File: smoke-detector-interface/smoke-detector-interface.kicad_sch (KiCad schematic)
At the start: 28 parts, among them J1 Conn_01x04_Pin, J2 M50-3500542, J3 DE9_Receptacle, J4 61200621621, J5 Conn_01x06_Pin, U1 UA78L10ACLPRE3, U2 AS7805AT, U3 ATtiny13A-P

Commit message: WIP
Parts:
- JP1: footprint TestPoint:TestPoint_Bridge_Pitch2.54mm_Drill0.7mm -> Resistor_THT:R_Axial_DIN0204_L3.6mm_D1.6mm_P7.62mm_Horizontal
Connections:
- net HOSTRX: now also J5.4 (Pin_4); no longer JP1.1 (A)
- net HOSTTX: now also JP1.1 (A); no longer J5.3 (Pin_3)
- net at JP1.2 (B): now also J5.3 (Pin_3); no longer J5.4 (Pin_4)
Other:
- moved on the sheet: JP1
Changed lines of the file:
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@@
 	(wire
 		(pts
-			(xy 196.85 143.51) (xy 194.31 143.51)
+			(xy 194.31 143.51) (xy 208.28 143.51)
 		)
 		(stroke
@@
 	(wire
 		(pts
-			(xy 208.28 140.97) (xy 196.85 140.97)
+			(xy 208.28 140.97) (xy 207.01 140.97)
 		)
 		(stroke
@@
 	(wire
 		(pts
-			(xy 208.28 143.51) (xy 207.01 143.51)
-		)
-		(stroke
-			(width 0)
-			(type default)
-		)
-	)
-	(wire
-		(pts
 			(xy 231.14 88.9) (xy 231.14 91.44)
 		)
@@
 	(symbol
 		(lib_id "Jumper:Jumper_2_Open")
-		(at 201.93 143.51 0)
+		(at 201.93 140.97 0)
 		(unit 1)
 		(exclude_from_sim yes)
@@
 		(fields_autoplaced yes)
 		(property "Reference" "JP1"
-			(at 201.93 137.16 0)
+			(at 201.93 134.62 0)
 			(effects
 				(font
@@
 		)
 		(property "Value" "Jumper_2_Open"
-			(at 201.93 139.7 0)
+			(at 201.93 137.16 0)
 			(effects
 				(font
@@
 			)
 		)
-		(property "Footprint" "TestPoint:TestPoint_Bridge_Pitch2.54mm_Drill0.7mm"
-			(at 201.93 143.51 0)
+		(property "Footprint" "Resistor_THT:R_Axial_DIN0204_L3.6mm_D1.6mm_P7.62mm_Horizontal"
+			(at 201.93 140.97 0)
 			(effects
 				(font
@@
 		)
 		(property "Datasheet" "~"
-			(at 201.93 143.51 0)
+			(at 201.93 140.97 0)
 			(effects
 				(font
@@
 		)
 		(property "Description" "Jumper, 2-pole, open"
-			(at 201.93 143.51 0)
+			(at 201.93 140.97 0)
 			(effects
 				(font

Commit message: Improved routing.
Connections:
- net _RESET: now also J4.5, U3.1 (~{RESET}/PB5)
- net MOSI: now reaches J4.4, U3.5 (PB0)
- net MISO: now reaches J4.1, U3.6 (PB1)
- net SCK: now reaches J4.3, U3.7 (PB2)
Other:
- moved on the sheet: J4, J5, JP1

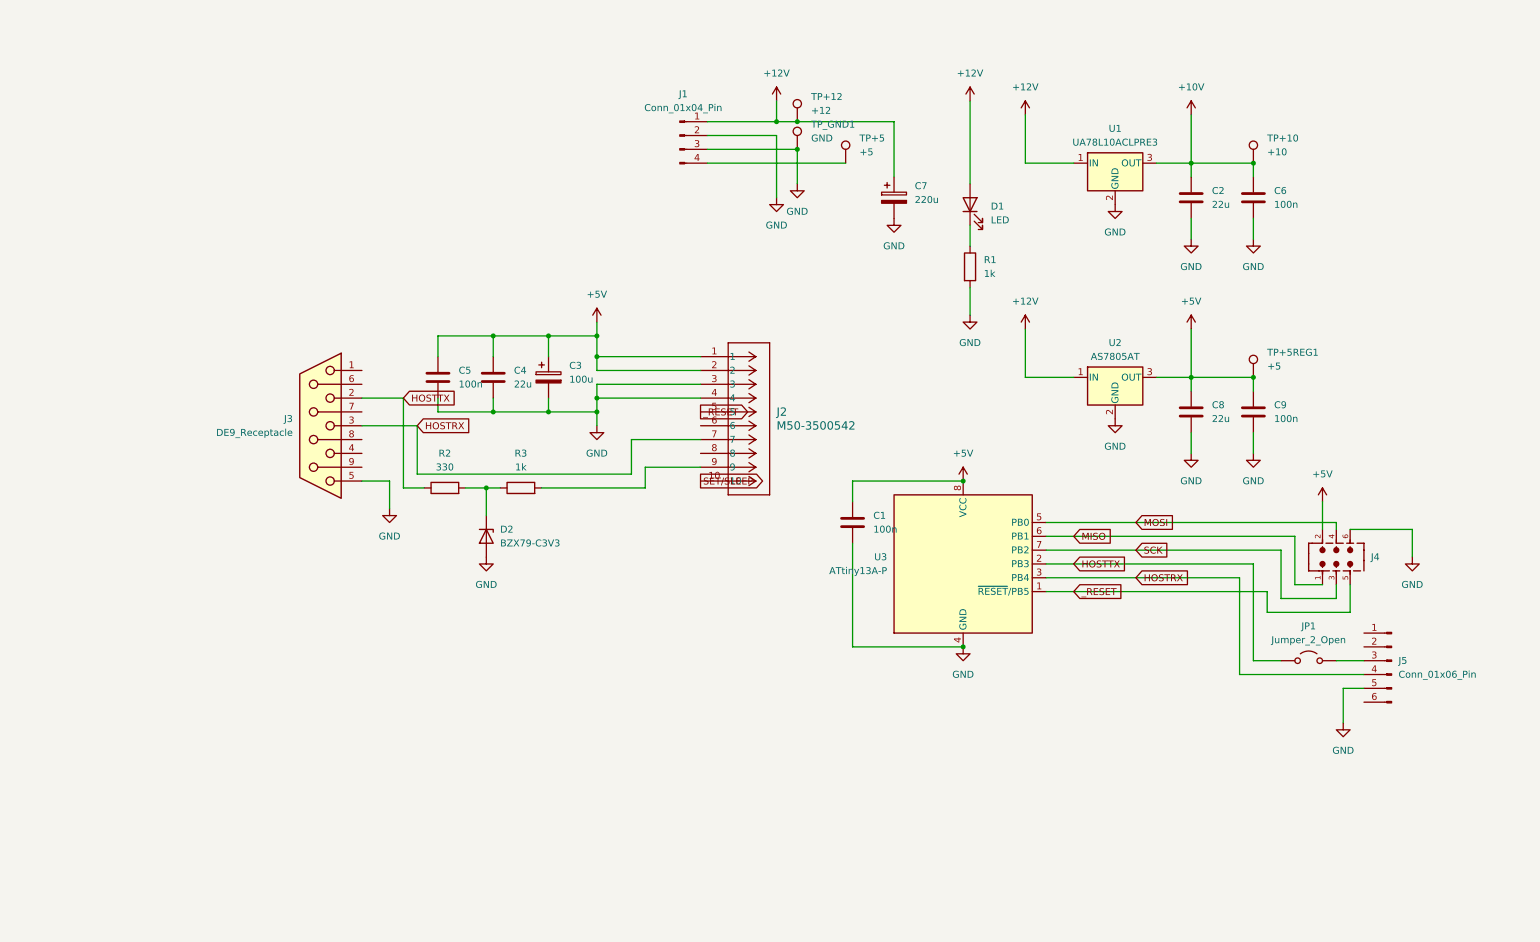
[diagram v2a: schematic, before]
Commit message: Updates for Zenerglass parts.
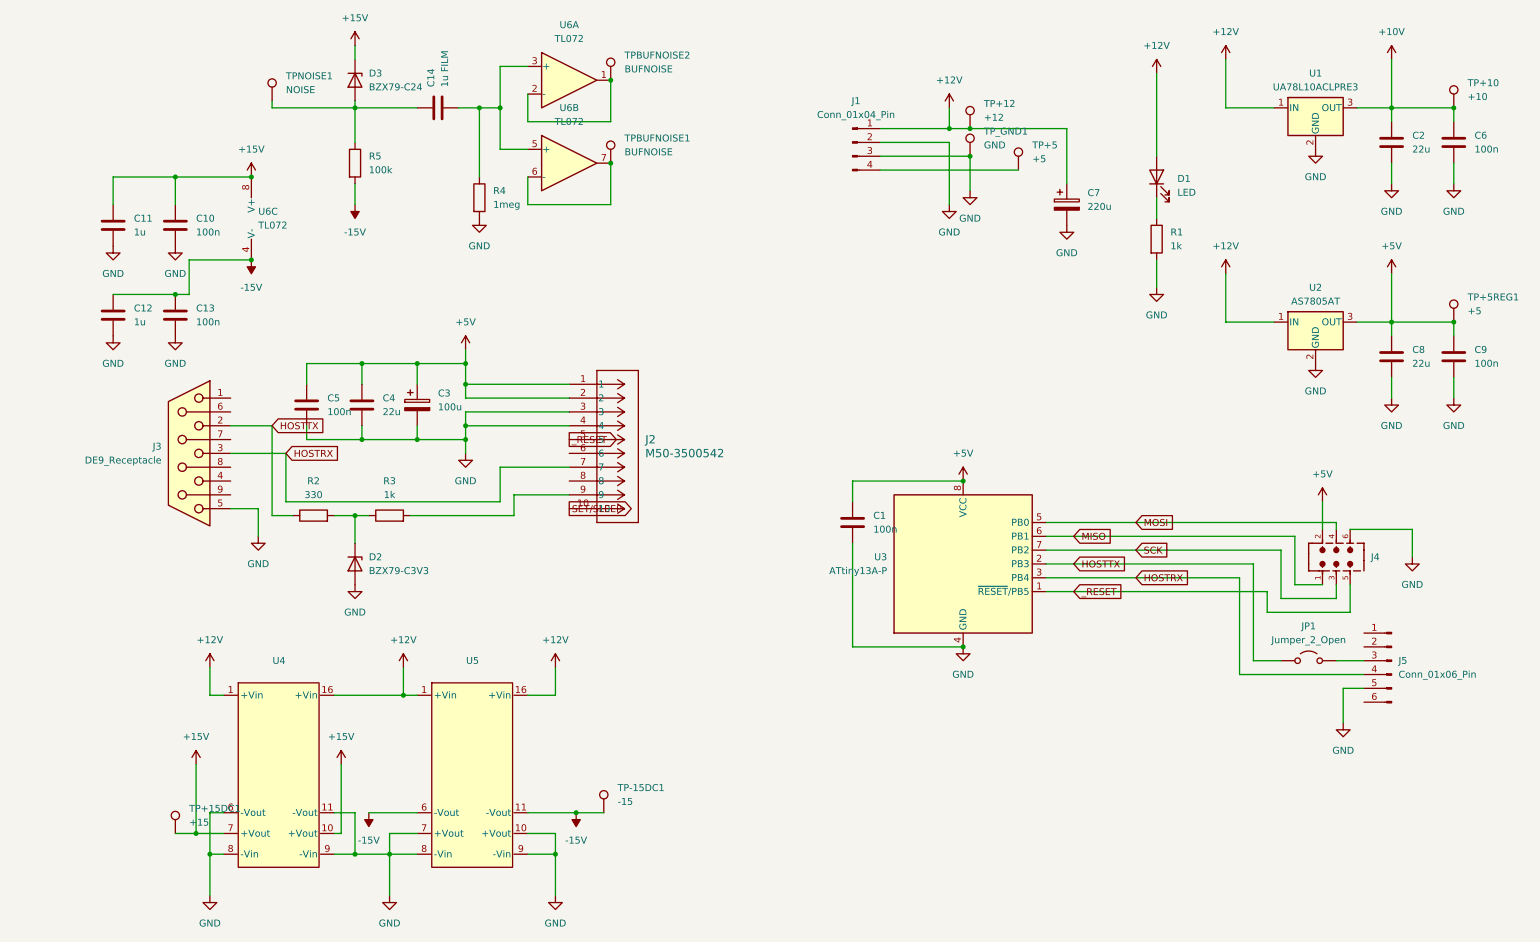
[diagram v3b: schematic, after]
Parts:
- added C10, C13: 100n, Capacitor_THT:C_Disc_D4.3mm_W1.9mm_P5.00mm, symbol Device:C
- added C11, C12: 1u, Capacitor_THT:C_Disc_D4.3mm_W1.9mm_P5.00mm, symbol Device:C
- added C14: 1u FILM, Capacitor_THT:C_Disc_D4.3mm_W1.9mm_P5.00mm, symbol Device:C
- added D3: BZX79-C24, Diode_THT:D_DO-35_SOD27_P12.70mm_Horizontal, symbol Device:D_Zener
- added R4: 1meg, Resistor_THT:R_Axial_DIN0207_L6.3mm_D2.5mm_P10.16mm_Horizontal, symbol Device:R
- added R5: 100k, Resistor_THT:R_Axial_DIN0207_L6.3mm_D2.5mm_P10.16mm_Horizontal, symbol Device:R
- added TP+15DC1: +15, TestPoint:TestPoint_THTPad_2.5x2.5mm_Drill1.2mm, symbol Connector:TestPoint
- added TP-15DC1: -15, TestPoint:TestPoint_THTPad_2.5x2.5mm_Drill1.2mm, symbol Connector:TestPoint
- added TPBUFNOISE1, TPBUFNOISE2: BUFNOISE, TestPoint:TestPoint_THTPad_2.5x2.5mm_Drill1.2mm, symbol Connector:TestPoint
- added TPNOISE1: NOISE, TestPoint:TestPoint_THTPad_2.5x2.5mm_Drill1.2mm, symbol Connector:TestPoint
- added U4, U5: ~, Package_DIP:DIP-16_W7.62mm_Socket, symbol ThirdPartySymbols:SRS-1215-2
- added U6: TL072, Package_DIP:DIP-8_W7.62mm_Socket, symbol Amplifier_Operational:TL072
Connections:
- net +12V: now also U4.1 (+Vin), U4.16 (+Vin), U5.1 (+Vin), U5.16 (+Vin)
- net GND: now also C10.2, C11.2, C12.2, C13.2, R4.2, U4.11 (-Vout), U4.6 (-Vout), U4.8 (-Vin), U4.9 (-Vin), U5.10 (+Vout), U5.7 (+Vout), U5.8 (-Vin), U5.9 (-Vin)
- new net: C14.2, R4.1, U6.3 (+), U6.5 (+)
- new net: TPBUFNOISE1.1, U6.6 (-), U6.7
- new net: C14.1, D3.2 (A), R5.1, TPNOISE1.1
- new net: TPBUFNOISE2.1, U6.1, U6.2 (-)
- new net +15V: C10.1, C11.1, D3.1 (K), TP+15DC1.1, U4.10 (+Vout), U4.7 (+Vout), U6.8 (V+)
- new net -15V: C12.1, C13.1, R5.2, TP-15DC1.1, U5.11 (-Vout), U5.6 (-Vout), U6.4 (V-)
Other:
- moved on the sheet: C2, C3, C4, C5, C6, C7, C8, C9, D1, D2, J1, J2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

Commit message: Add mounting holes.
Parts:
- added H1, H2: MountingHole, MountingHole:MountingHole_3.2mm_M3, symbol Mechanical:MountingHole
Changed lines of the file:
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@@
 	)
 	(symbol
+		(lib_id "Mechanical:MountingHole")
+		(at 22.86 30.48 0)
+		(unit 1)
+		(exclude_from_sim yes)
+		(in_bom no)
+		(on_board yes)
+		(dnp no)
+		(fields_autoplaced yes)
+		(property "Reference" "H2"
+			(at 25.4 29.2099 0)
+			(effects
+				(font
+					(size 1.27 1.27)
+				)
+				(justify left)
+			)
+		)
+		(property "Value" "MountingHole"
+			(at 25.4 31.7499 0)
+			(effects
+				(font
+					(size 1.27 1.27)
+				)
+				(justify left)
+			)
+		)
+		(property "Footprint" "MountingHole:MountingHole_3.2mm_M3"
+			(at 22.86 30.48 0)
+			(effects
+				(font
+					(size 1.27 1.27)
+				)
+				(hide yes)
+			)
+		)
+		(property "Datasheet" "~"
+			(at 22.86 30.48 0)
+			(effects
+				(font
+					(size 1.27 1.27)
+				)
+				(hide yes)
+			)
+		)
+		(property "Description" "Mounting Hole without connection"
+			(at 22.86 30.48 0)
+			(effects
+				(font
+					(size 1.27 1.27)
+				)
+				(hide yes)
+			)
+		)
+		(instances
+			(project "smoke-detector-interface"
+				(path "/c29341ff-72d1-44fb-b26d-485fe5ca1842"
+					(reference "H2")
+					(unit 1)
+				)
+			)
+		)
+	)
+	(symbol
 		(lib_id "Amplifier_Operational:TL072")
 		(at 105.41 34.29 0)
@@
 					(unit 1)
 				)
+			)
+		)
+	)
+	(symbol
+		(lib_id "Mechanical:MountingHole")
+		(at 22.86 24.13 0)
+		(unit 1)
+		(exclude_from_sim yes)
+		(in_bom no)
+		(on_board yes)
+		(dnp no)
+		(fields_autoplaced yes)
+		(property "Reference" "H1"
+			(at 25.4 22.8599 0)
+			(effects
+				(font
+					(size 1.27 1.27)
+				)
+				(justify left)
+			)
+		)
+		(property "Value" "MountingHole"
+			(at 25.4 25.3999 0)
+			(effects
+				(font
+					(size 1.27 1.27)
+				)
+				(justify left)
+			)
+		)
+		(property "Footprint" "MountingHole:MountingHole_3.2mm_M3"
+			(at 22.86 24.13 0)
+			(effects
+				(font
+					(size 1.27 1.27)
+				)
+				(hide yes)
+			)
+		)
+		(property "Datasheet" "~"
+			(at 22.86 24.13 0)
+			(effects
+				(font
+					(size 1.27 1.27)
+				)
+				(hide yes)
+			)
+		)
+		(property "Description" "Mounting Hole without connection"
+			(at 22.86 24.13 0)
+			(effects
+				(font
+					(size 1.27 1.27)
+				)
+				(hide yes)
+			)
+		)
+		(instances
+			(project ""
+				(path "/c29341ff-72d1-44fb-b26d-485fe5ca1842"
+					(reference "H1")
+					(unit 1)
+				)

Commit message: DRC passes.
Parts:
- removed C2: 22u, Capacitor_THT:CP_Radial_D5.0mm_P2.00mm, symbol Device:C
- removed C6: 100n, Capacitor_THT:C_Disc_D4.3mm_W1.9mm_P5.00mm, symbol Device:C
- removed TP+10: +10, TestPoint:TestPoint_THTPad_2.5x2.5mm_Drill1.2mm, symbol Connector:TestPoint
- removed U1: UA78L10ACLPRE3, Package_TO_SOT_THT:TO-92_HandSolder, symbol Regulator_Linear:L7805
- added D4, D5: LED, LED_THT:LED_D5.0mm, symbol Device:LED
- added R6, R7: 1k, Resistor_THT:R_Axial_DIN0207_L6.3mm_D2.5mm_P10.16mm_Horizontal, symbol Device:R
- C11, C12: footprint Capacitor_THT:C_Disc_D4.3mm_W1.9mm_P5.00mm -> Capacitor_THT:C_Disc_D3.8mm_W2.6mm_P2.50mm
- C14: value 1u FILM -> .47u FILM; footprint Capacitor_THT:C_Disc_D4.3mm_W1.9mm_P5.00mm -> Capacitor_THT:C_Rect_L7.2mm_W3.5mm_P5.00mm_FKS2_FKP2_MKS2_MKP2
- J5: footprint Connector_PinSocket_2.54mm:PinSocket_1x06_P2.54mm_Vertical -> Connector_PinHeader_2.54mm:PinHeader_1x06_P2.54mm_Vertical
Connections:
- net +15V: now also D4.2 (A)
- net -15V: now also D5.1 (K)
- net GND: now also R6.2, R7.1
- new net: D5.2 (A), R7.2
- new net: D4.1 (K), R6.1

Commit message: Add jumpers to serial rx/tx in case they need swapping.
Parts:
- added JP2, JP3, JP4: Jumper_2_Open, Resistor_THT:R_Axial_DIN0204_L3.6mm_D1.6mm_P7.62mm_Horizontal, symbol Jumper:Jumper_2_Open
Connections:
- net HOSTRX: now also JP4.2 (B); no longer J3.3
- net HOSTTX: now also JP2.1 (A), JP3.2 (B); no longer J3.2
- net BUFFERED_NOISE: now reaches TPBUFNOISE1.1, U6.6 (-), U6.7
- net BUFFERED_NOISE: now also JP2.2 (B)
- new net: J3.3, JP4.1 (A)
- new net: J3.2, JP3.1 (A)
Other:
- moved on the sheet: J3

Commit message: First production candidate.
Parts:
- added F1: Fuse, ThirdPartyFootprints:01530008, symbol Device:Fuse
- added TP12VIN1: +12, TestPoint:TestPoint_THTPad_2.5x2.5mm_Drill1.2mm, symbol Connector:TestPoint
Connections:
- net +12V: now also F1.2; no longer J1.1 (Pin_1)
- new net: F1.1, J1.1 (Pin_1), TP12VIN1.1
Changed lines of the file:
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@@
 	)
 	(junction
+		(at 165.1 43.18)
+		(diameter 0)
+		(color 0 0 0 0)
+	)
+	(junction
 		(at 72.39 176.53)
 		(diameter 0)
@@
 	(wire
 		(pts
+			(xy 173.99 43.18) (xy 175.26 43.18)
+		)
+		(stroke
+			(width 0)
+			(type default)
+		)
+	)
+	(wire
+		(pts
 			(xy 74.93 147.32) (xy 77.47 147.32)
 		)
@@
 	(wire
 		(pts
-			(xy 162.56 43.18) (xy 175.26 43.18)
+			(xy 162.56 43.18) (xy 165.1 43.18)
 		)
 		(stroke
@@
 	(wire
 		(pts
+			(xy 165.1 30.48) (xy 165.1 43.18)
+		)
+		(stroke
+			(width 0)
+			(type default)
+		)
+	)
+	(wire
+		(pts
 			(xy 97.79 41.91) (xy 97.79 36.83)
 		)
@@
 	(wire
 		(pts
+			(xy 165.1 43.18) (xy 166.37 43.18)
+		)
+		(stroke
+			(width 0)
+			(type default)
+		)
+	)
+	(wire
+		(pts
 			(xy 223.52 100.33) (xy 220.98 100.33)
 		)
@@
 		)
 	)
+	(netclass_flag ""
+		(length 2.54)
+		(shape round)
+		(at 165.1 34.29 90)
+		(fields_autoplaced yes)
+		(effects
+			(font
+				(size 1.27 1.27)
+			)
+			(justify left bottom)
+		)
+		(property "Netclass" "Power"
+			(at 162.56 33.5915 90)
+			(effects
+				(font
+					(size 1.27 1.27)
+					(italic yes)
+				)
+				(justify left)
+			)
+		)
+	)
 	(symbol
 		(lib_id "Amplifier_Operational:TL072")
@@
 	)
 	(symbol
+		(lib_id "Device:Fuse")
+		(at 170.18 43.18 90)
+		(unit 1)
+		(exclude_from_sim no)
+		(in_bom yes)
+		(on_board yes)
+		(dnp no)
+		(fields_autoplaced yes)
+		(property "Reference" "F1"
+			(at 170.18 36.83 90)
+			(effects
+				(font
+					(size 1.27 1.27)
+				)
+			)
+		)
+		(property "Value" "Fuse"
+			(at 170.18 39.37 90)
+			(effects
+				(font
+					(size 1.27 1.27)
+				)
+			)
+		)
+		(property "Footprint" "ThirdPartyFootprints:01530008"
+			(at 170.18 44.958 90)
+			(effects
+				(font
+					(size 1.27 1.27)
+				)
+				(hide yes)
+			)
+		)
+		(property "Datasheet" "~"
+			(at 170.18 43.18 0)
+			(effects
+				(font
+					(size 1.27 1.27)
+				)
+				(hide yes)
+			)
+		)
+		(property "Description" ""
+			(at 170.18 43.18 0)
+			(effects
+				(font
+					(size 1.27 1.27)
+				)
+				(hide yes)
+			)
+		)
+		(pin "2"
+		)
+		(pin "1"
+		)
+		(instances
+			(project "smoke-detector-interface"
+				(path "/c29341ff-72d1-44fb-b26d-485fe5ca1842"
+					(reference "F1")
+					(unit 1)
+				)
+			)
+		)
+	)
+	(symbol
 		(lib_id "Device:R")
 		(at 88.9 55.88 0)
@@
 					(unit 1)
 				)
+			)
+		)
+	)
+	(symbol
+		(lib_id "Connector:TestPoint")
+		(at 165.1 30.48 0)
+		(unit 1)
+		(exclude_from_sim no)
+		(in_bom yes)
+		(on_board yes)
+		(dnp no)
+		(property "Reference" "TP12VIN1"
+			(at 167.64 25.908 0)
+			(effects
+				(font
+					(size 1.27 1.27)
+				)
+				(justify left)
+			)
+		)
+		(property "Value" "+12"
+			(at 167.64 28.448 0)
+			(effects
+				(font
+					(size 1.27 1.27)
+				)
+				(justify left)
+			)
+		)
+		(property "Footprint" "TestPoint:TestPoint_THTPad_2.5x2.5mm_Drill1.2mm"
+			(at 170.18 30.48 0)
+			(effects
+				(font
+					(size 1.27 1.27)
+				)
+				(hide yes)
+			)
+		)
+		(property "Datasheet" "~"
+			(at 170.18 30.48 0)
+			(effects
+				(font
+					(size 1.27 1.27)
+				)
+				(hide yes)
+			)
+		)
+		(property "Description" "test point"
+			(at 165.1 30.48 0)
+			(effects
+				(font
+					(size 1.27 1.27)
+				)
+				(hide yes)
+			)
+		)
+		(pin "1"
+		)
+		(instances
+			(project "smoke-detector-interface"
+				(path "/c29341ff-72d1-44fb-b26d-485fe5ca1842"
+					(reference "TP12VIN1")
+					(unit 1)
+				)
